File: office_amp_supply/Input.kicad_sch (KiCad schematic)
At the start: 23 parts, among them J2 Conn_01x03_Female, J3 Conn_02x07_Odd_Even, J4 Conn_01x03_Female, J8 Conn_01x03_Female, K1 V23079-A1003-B301, K2 V23079-A1003-B301, K3 V23079-A1003-B301, K4 V23079-A1003-B301, Q4 BC850, Q5 BC850

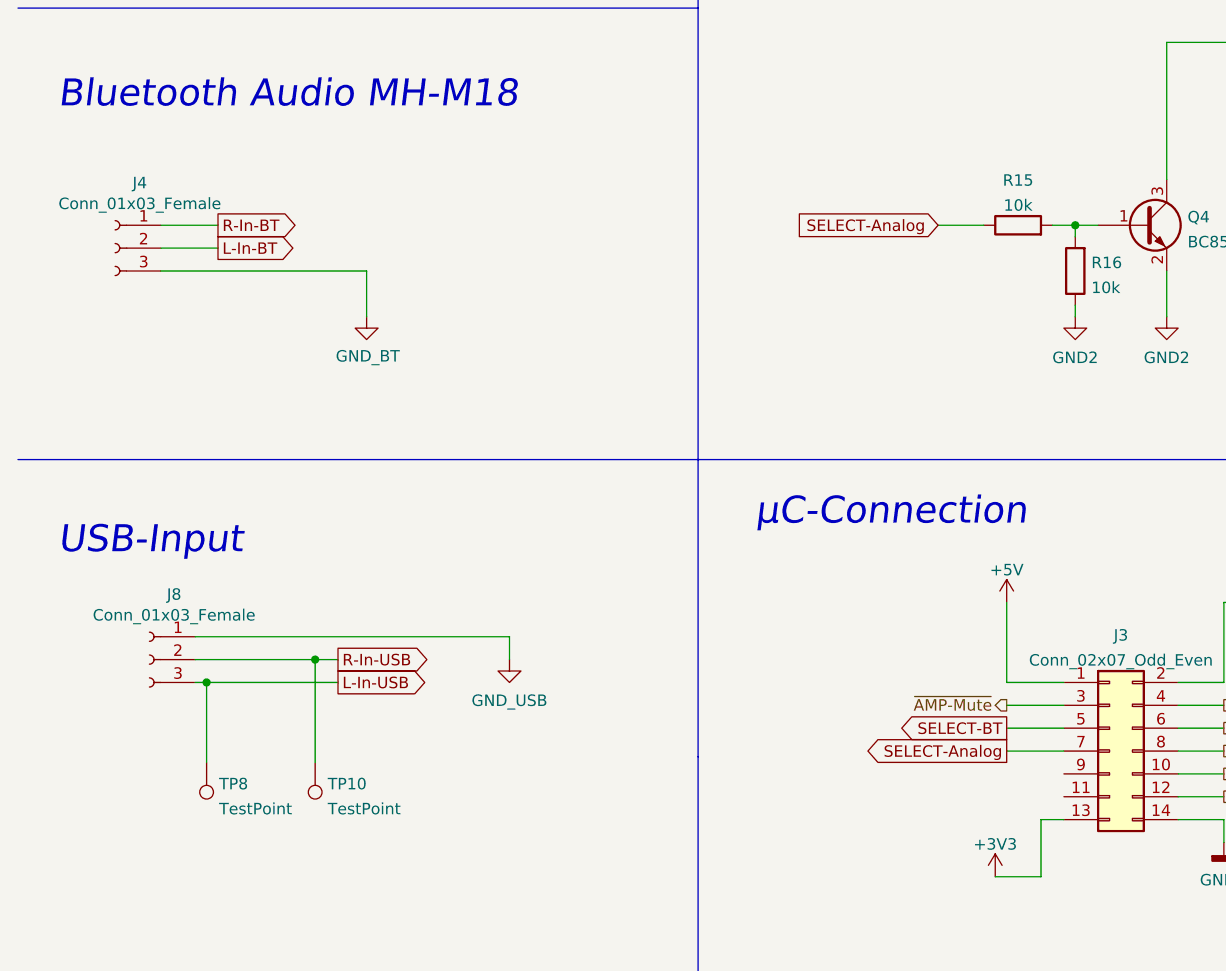
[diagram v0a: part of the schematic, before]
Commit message: splitted the prototype in 2 PCBs
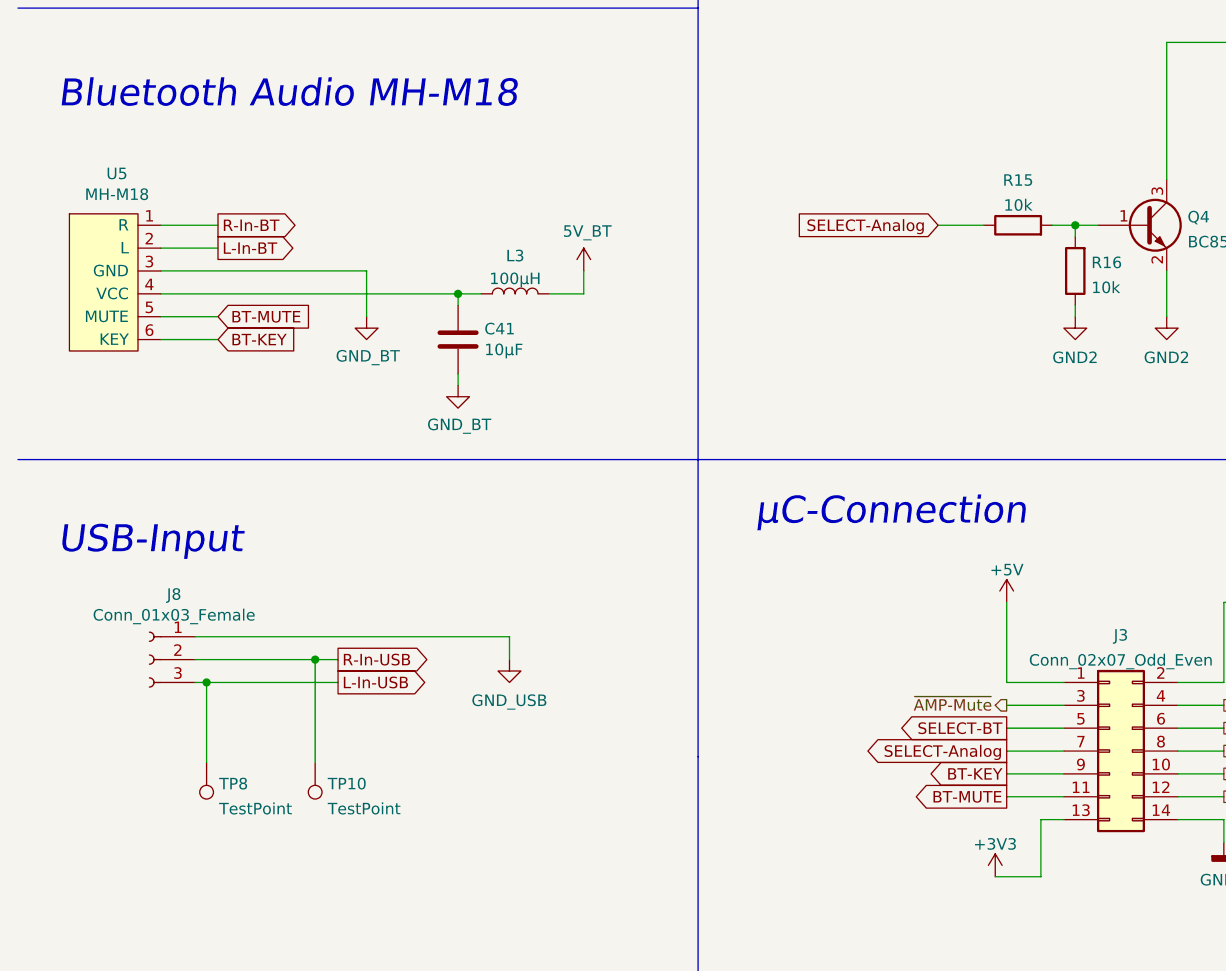
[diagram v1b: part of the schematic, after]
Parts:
- removed J4: Conn_01x03_Female, Connector_PinHeader_2.54mm:PinHeader_1x03_P2.54mm_Vertical, symbol Connector:Conn_01x03_Female
- added C41: 10µF, Capacitor_SMD:C_0805_2012Metric_Pad1.18x1.45mm_HandSolder, symbol Device:C
- added L3: 100µH, Inductor_THT:L_Axial_L7.0mm_D3.3mm_P12.70mm_Horizontal_Fastron_MICC, symbol Device:L
- added U5: MH-M18, MyLib:MH-M18, symbol MyLib:MH-M18
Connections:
- net 5V_BT: now also L3.2
- net GND_BT: now also C41.2, U5.3 (GND)
- net L-In-BT: now also U5.2 (L)
- net R-In-BT: now also U5.1 (R)
- net BT-MUTE: now reaches J3.11 (Pin_11)
- net BT-MUTE: now also U5.5 (MUTE)
- net BT-KEY: now reaches J3.9 (Pin_9)
- net BT-KEY: now also U5.6 (KEY)
- new net: C41.1, L3.1, U5.4 (VCC)
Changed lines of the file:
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@@
   (junction (at 58.42 35.56) (diameter 0) (color 0 0 0 0)
   )
+  (junction (at 60.96 100.33) (diameter 0) (color 0 0 0 0)
+  )
   (junction (at 195.58 40.64) (diameter 0) (color 0 0 0 0)
   )
@@
     (stroke (width 0) (type default))
   )
+  (wire (pts (xy 121.92 153.67) (xy 128.27 153.67))
+    (stroke (width 0) (type default))
+  )
   (wire (pts (xy 106.68 63.5) (xy 107.95 63.5))
     (stroke (width 0) (type default))
@@
     (stroke (width 0) (type default))
   )
+  (wire (pts (xy 27.94 100.33) (xy 60.96 100.33))
+    (stroke (width 0) (type default))
+  )
+  (wire (pts (xy 27.94 102.87) (xy 34.29 102.87))
+    (stroke (width 0) (type default))
+  )
   (wire (pts (xy 193.04 64.77) (xy 193.04 63.5))
     (stroke (width 0) (type default))
@@
     (stroke (width 0) (type default))
   )
+  (wire (pts (xy 60.96 100.33) (xy 63.5 100.33))
+    (stroke (width 0) (type default))
+  )
+  (wire (pts (xy 60.96 109.22) (xy 60.96 110.49))
+    (stroke (width 0) (type default))
+  )
   (wire (pts (xy 215.9 50.8) (xy 215.9 49.53))
     (stroke (width 0) (type default))
@@
     (stroke (width 0) (type default))
   )
+  (wire (pts (xy 74.93 97.79) (xy 74.93 100.33))
+    (stroke (width 0) (type default))
+  )
   (wire (pts (xy 140.97 151.13) (xy 146.05 151.13))
     (stroke (width 0) (type default))
@@
     (stroke (width 0) (type default))
   )
+  (wire (pts (xy 71.12 100.33) (xy 74.93 100.33))
+    (stroke (width 0) (type default))
+  )
   (wire (pts (xy 46.355 33.02) (xy 64.77 33.02))
     (stroke (width 0) (type default))
@@
     (stroke (width 0) (type default))
   )
+  (wire (pts (xy 60.96 100.33) (xy 60.96 101.6))
+    (stroke (width 0) (type default))
+  )
   (wire (pts (xy 255.27 96.52) (xy 255.27 93.98))
     (stroke (width 0) (type default))
@@
     (stroke (width 0) (type default))
   )
+  (wire (pts (xy 121.92 156.21) (xy 128.27 156.21))
+    (stroke (width 0) (type default))
+  )
   (polyline (pts (xy 87.63 118.745) (xy 87.63 68.58))
     (stroke (width 0) (type default))
   )
   (wire (pts (xy 171.45 40.64) (xy 176.53 40.64))
+    (stroke (width 0) (type default))
+  )
+  (wire (pts (xy 27.94 105.41) (xy 34.29 105.41))
     (stroke (width 0) (type default))
   )
@@
     )
   )
+  (global_label "BT-MUTE" (shape input) (at 34.29 102.87 0) (fields_autoplaced)
+    (effects (font (size 1.27 1.27)) (justify left))
+    (property "Intersheetrefs" "${INTERSHEET_REFS}" (at 1.27 -5.08 0)
+      (effects (font (size 1.27 1.27)) hide)
+    )
+  )
+  (global_label "BT-KEY" (shape output) (at 121.92 153.67 180) (fields_autoplaced)
+    (effects (font (size 1.27 1.27)) (justify right))
+    (property "Intersheetrefs" "${INTERSHEET_REFS}" (at 112.2782 153.5906 0)
+      (effects (font (size 1.27 1.27)) (justify right) hide)
+    )
+  )
   (global_label "L-In-USB" (shape output) (at 47.625 143.51 0) (fields_autoplaced)
     (effects (font (size 1.27 1.27)) (justify left))
@@
     (property "Intersheetrefs" "${INTERSHEET_REFS}" (at -13.97 -16.51 0)
       (effects (font (size 1.27 1.27)) hide)
+    )
+  )
+  (global_label "BT-MUTE" (shape output) (at 121.92 156.21 180) (fields_autoplaced)
+    (effects (font (size 1.27 1.27)) (justify right))
+    (property "Intersheetrefs" "${INTERSHEET_REFS}" (at 110.8872 156.1306 0)
+      (effects (font (size 1.27 1.27)) (justify right) hide)
     )
   )
@@
     )
   )
+  (global_label "BT-KEY" (shape input) (at 34.29 105.41 0) (fields_autoplaced)
+    (effects (font (size 1.27 1.27)) (justify left))
+    (property "Intersheetrefs" "${INTERSHEET_REFS}" (at 1.27 -5.08 0)
+      (effects (font (size 1.27 1.27)) hide)
+    )
+  )
   (global_label "SELECT-Analog" (shape output) (at 121.92 151.13 180) (fields_autoplaced)
     (effects (font (size 1.27 1.27)) (justify right))
@@
   (hierarchical_label "AMP-GAIN1" (shape output) (at 146.05 151.13 0) (fields_autoplaced)
     (effects (font (size 1.27 1.27)) (justify left))
+  )
+  (symbol (lib_id "MyLib:MH-M18") (at 21.59 99.06 0) (unit 1)
+    (in_bom yes) (on_board yes) (dnp no)
+    (property "Reference" "U5" (at 23.0632 86.995 0)
+      (effects (font (size 1.27 1.27)))
+    )
+    (property "Value" "MH-M18" (at 23.0632 89.3064 0)
+      (effects (font (size 1.27 1.27)))
+    )
+    (property "Footprint" "MyLib:MH-M18" (at 24.13 107.95 0)
+      (effects (font (size 1.27 1.27)) hide)
+    )
+    (property "Datasheet" "" (at 31.75 102.87 0)
+      (effects (font (size 1.27 1.27)) hide)
+    )
+    (pin "1")
+    (pin "2")
+    (pin "3")
+    (pin "4")
+    (pin "5")
+    (pin "6")
+    (instances
+      (project "office_amp"
+        (path "/2de1ffee-2174-41d2-8969-68b8d21e5a7d/00000000-0000-0000-0000-00005ed110e5"
+          (reference "U5") (unit 1)
+        )
+      )
+    )
+  )
+  (symbol (lib_id "OfficeAmp:5V_BT") (at 74.93 97.79 0) (unit 1)
+    (in_bom yes) (on_board yes) (dnp no)
+    (property "Reference" "#PWR0137" (at 74.93 101.6 0)
+      (effects (font (size 1.27 1.27)) hide)
+    )
+    (property "Value" "5V_BT" (at 75.311 93.3958 0)
+      (effects (font (size 1.27 1.27)))
+    )
+    (property "Footprint" "" (at 74.93 97.79 0)
+      (effects (font (size 1.27 1.27)) hide)
+    )
+    (property "Datasheet" "" (at 74.93 97.79 0)
+      (effects (font (size 1.27 1.27)) hide)
+    )
+    (pin "1")
+    (instances
+      (project "office_amp"
+        (path "/2de1ffee-2174-41d2-8969-68b8d21e5a7d/00000000-0000-0000-0000-00005ed110e5"
+          (reference "#PWR0137") (unit 1)
+        )
+      )
+    )
   )
   (symbol (lib_id "Relay:EC2-24NU") (at 115.57 50.8 90) (mirror x) (unit 1)
@@
     )
   )
+  (symbol (lib_id "Device:L") (at 67.31 100.33 90) (unit 1)
+    (in_bom yes) (on_board yes) (dnp no) (fields_autoplaced)
+    (property "Reference" "L3" (at 67.31 96.1222 90)
+      (effects (font (size 1.27 1.27)))
+    )
+    (property "Value" "100µH" (at 67.31 98.6591 90)
+      (effects (font (size 1.27 1.27)))
+    )
+    (property "Footprint" "Inductor_THT:L_Axial_L7.0mm_D3.3mm_P12.70mm_Horizontal_Fastron_MICC" (at 67.31 100.33 0)
+      (effects (font (size 1.27 1.27)) hide)
+    )
+    (property "Datasheet" "~" (at 67.31 100.33 0)
+      (effects (font (size 1.27 1.27)) hide)
+    )
+    (pin "1")
+    (pin "2")
+    (instances
+      (project "office_amp"
+        (path "/2de1ffee-2174-41d2-8969-68b8d21e5a7d/00000000-0000-0000-0000-00005ed110e5"
+          (reference "L3") (unit 1)
+        )
+      )
+    )
+  )
   (symbol (lib_id "Transistor_BJT:BC850") (at 223.52 92.71 0) (unit 1)
     (in_bom yes) (on_board yes) (dnp no) (fields_autoplaced)
@@
     )
   )
-  (symbol (lib_id "Connector:Conn_01x03_Female") (at 22.86 95.25 0) (mirror y) (unit 1)
-    (in_bom yes) (on_board yes) (dnp no)
-    (property "Reference" "J4" (at 25.6032 88.011 0)
-      (effects (font (size 1.27 1.27)))
-    )
-    (property "Value" "Conn_01x03_Female" (at 25.6032 90.3224 0)
-      (effects (font (size 1.27 1.27)))
-    )
-    (property "Footprint" "Connector_PinHeader_2.54mm:PinHeader_1x03_P2.54mm_Vertical" (at 22.86 95.25 0)
-      (effects (font (size 1.27 1.27)) hide)
-    )
-    (property "Datasheet" "~" (at 22.86 95.25 0)
-      (effects (font (size 1.27 1.27)) hide)
-    )
-    (pin "1")
-    (pin "2")
-    (pin "3")
-    (instances
-      (project "office_amp"
-        (path "/2de1ffee-2174-41d2-8969-68b8d21e5a7d/00000000-0000-0000-0000-00005ed110e5"
-          (reference "J4") (unit 1)
-        )
-      )
-    )
-  )
   (symbol (lib_id "power:GNDREF") (at 255.27 96.52 0) (unit 1)
     (in_bom yes) (on_board yes) (dnp no) (fields_autoplaced)
@@
     )
   )
+  (symbol (lib_id "Device:C") (at 60.96 105.41 0) (unit 1)
+    (in_bom yes) (on_board yes) (dnp no)
+    (property "Reference" "C41" (at 63.881 104.2416 0)
+      (effects (font (size 1.27 1.27)) (justify left))
+    )
+    (property "Value" "10µF" (at 63.881 106.553 0)
+      (effects (font (size 1.27 1.27)) (justify left))
+    )
+    (property "Footprint" "Capacitor_SMD:C_0805_2012Metric_Pad1.18x1.45mm_HandSolder" (at 61.9252 109.22 0)
+      (effects (font (size 1.27 1.27)) hide)
+    )
+    (property "Datasheet" "~" (at 60.96 105.41 0)
+      (effects (font (size 1.27 1.27)) hide)
+    )
+    (pin "1")
+    (pin "2")
+    (instances
+      (project "office_amp"
+        (path "/2de1ffee-2174-41d2-8969-68b8d21e5a7d/00000000-0000-0000-0000-00005ed110e5"
+          (reference "C41") (unit 1)
+        )
+      )
+    )
+  )
   (symbol (lib_id "power:GND2") (at 270.51 96.52 0) (unit 1)
     (in_bom yes) (on_board yes) (dnp no) (fields_autoplaced)
@@
         )
       )
+    )
+  )
+  (symbol (lib_id "OfficeAmp:GND_BT") (at 60.96 110.49 0) (unit 1)
+    (in_bom yes) (on_board yes) (dnp no)
+    (property "Reference" "#PWR04" (at 60.96 116.84 0)
+      (effects (font (size 1.27 1.27)) hide)
+    )
+    (property "Value" "GND_BT" (at 61.087 114.8842 0)
+      (effects (font (size 1.27 1.27)))
+    )
+    (property "Footprint" "" (at 60.96 110.49 0)
+      (effects (font (size 1.27 1.27)) hide)
+    )
+    (property "Datasheet" "" (at 60.96 110.49 0)
+      (effects (font (size 1.27 1.27)) hide)
+    )
+    (pin "1")
+    (instances
+      (project "office_amp"
+        (path "/2de1ffee-2174-41d2-8969-68b8d21e5a7d/00000000-0000-0000-0000-00005ed110e5"
+          (reference "#PWR04") (unit 1)
+        )
+      )
